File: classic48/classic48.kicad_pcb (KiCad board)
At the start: 2 copper layers, 3.4 x 3 mm, 5 parts, among them SW1 Switch, U1 RP2040_Pro_Micro, U2 TRRS

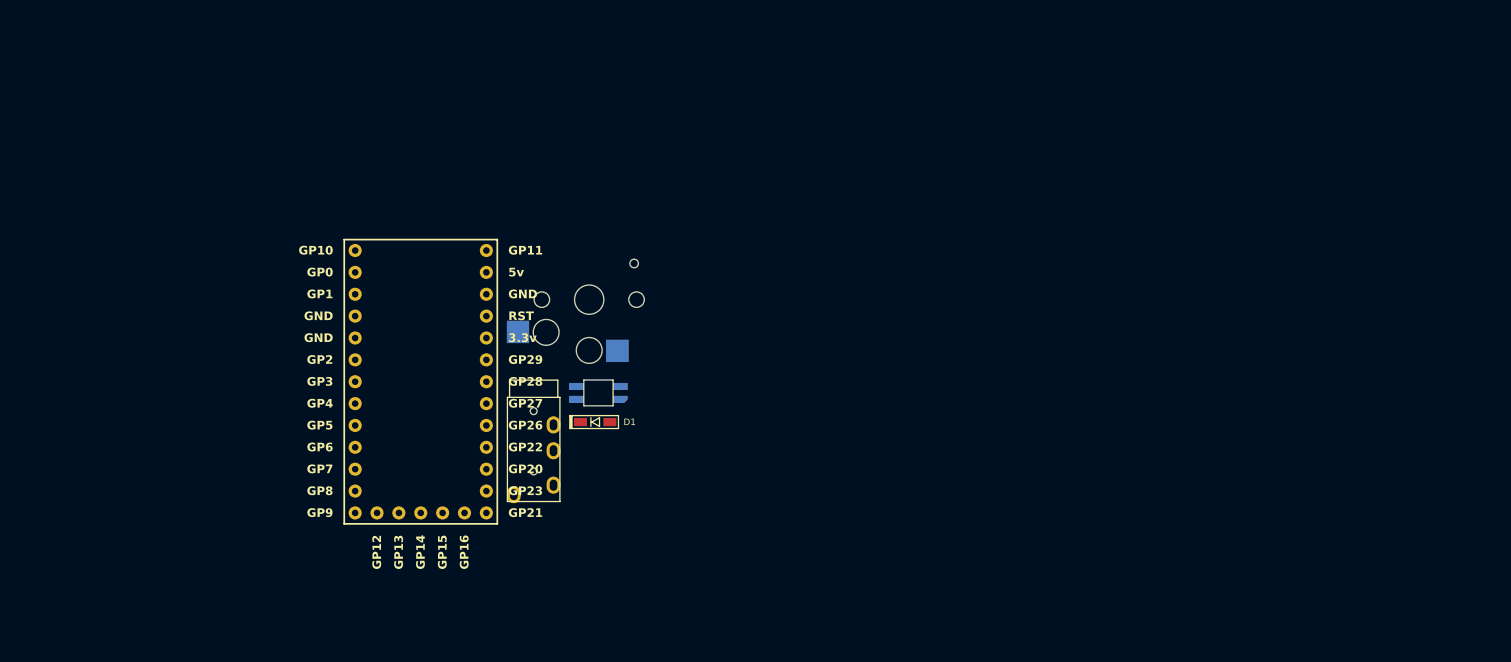
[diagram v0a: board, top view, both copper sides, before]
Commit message: feat: schematic for left side
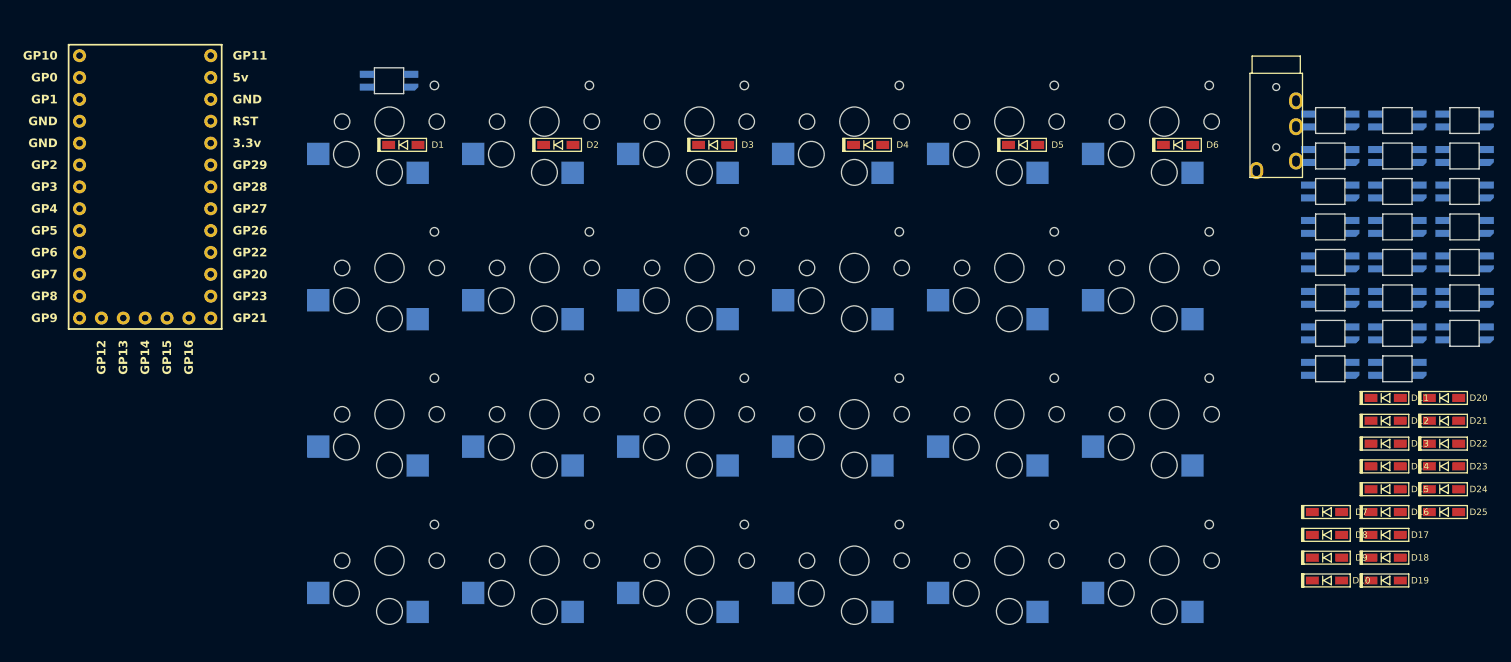
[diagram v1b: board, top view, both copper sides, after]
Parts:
- added D10: Diode_1N4148-SOD123, pjimenez:Diode_1N4148-SOD123, F.Cu at (165.9, 83.8)
- added D11: Diode_1N4148-SOD123, pjimenez:Diode_1N4148-SOD123, F.Cu at (172.7, 62.6)
- added D12: Diode_1N4148-SOD123, pjimenez:Diode_1N4148-SOD123, F.Cu at (172.7, 65.2)
- added D13: Diode_1N4148-SOD123, pjimenez:Diode_1N4148-SOD123, F.Cu at (172.7, 67.9)
- added D14: Diode_1N4148-SOD123, pjimenez:Diode_1N4148-SOD123, F.Cu at (172.7, 70.5)
- added D15: Diode_1N4148-SOD123, pjimenez:Diode_1N4148-SOD123, F.Cu at (172.7, 73.2)
- added D16: Diode_1N4148-SOD123, pjimenez:Diode_1N4148-SOD123, F.Cu at (172.7, 75.8)
- added D17: Diode_1N4148-SOD123, pjimenez:Diode_1N4148-SOD123, F.Cu at (172.7, 78.5)
- added D18: Diode_1N4148-SOD123, pjimenez:Diode_1N4148-SOD123, F.Cu at (172.7, 81.2)
- added D19: Diode_1N4148-SOD123, pjimenez:Diode_1N4148-SOD123, F.Cu at (172.7, 83.8)
- added D2: Diode_1N4148-SOD123, pjimenez:Diode_1N4148-SOD123, F.Cu at (76.6, 33.2)
- added D20: Diode_1N4148-SOD123, pjimenez:Diode_1N4148-SOD123, F.Cu at (179.5, 62.6)
- added D21: Diode_1N4148-SOD123, pjimenez:Diode_1N4148-SOD123, F.Cu at (179.5, 65.2)
- added D22: Diode_1N4148-SOD123, pjimenez:Diode_1N4148-SOD123, F.Cu at (179.5, 67.9)
- added D23: Diode_1N4148-SOD123, pjimenez:Diode_1N4148-SOD123, F.Cu at (179.5, 70.5)
- added D24: Diode_1N4148-SOD123, pjimenez:Diode_1N4148-SOD123, F.Cu at (179.5, 73.2)
- added D25: Diode_1N4148-SOD123, pjimenez:Diode_1N4148-SOD123, F.Cu at (179.5, 75.8)
- added D3: Diode_1N4148-SOD123, pjimenez:Diode_1N4148-SOD123, F.Cu at (94.6, 33.2)
- added D4: Diode_1N4148-SOD123, pjimenez:Diode_1N4148-SOD123, F.Cu at (112.6, 33.2)
- added D5: Diode_1N4148-SOD123, pjimenez:Diode_1N4148-SOD123, F.Cu at (130.6, 33.2)
- added D6: Diode_1N4148-SOD123, pjimenez:Diode_1N4148-SOD123, F.Cu at (148.6, 33.2)
- added D7: Diode_1N4148-SOD123, pjimenez:Diode_1N4148-SOD123, F.Cu at (165.9, 75.8)
- added D8: Diode_1N4148-SOD123, pjimenez:Diode_1N4148-SOD123, F.Cu at (165.9, 78.5)
- added D9: Diode_1N4148-SOD123, pjimenez:Diode_1N4148-SOD123, F.Cu at (165.9, 81.2)
- added LED10: LED_SK6812MINI-E, pjimenez:LED_SK6812-MINI-E, F.Cu at (174.1, 30.4)
- added LED11: LED_SK6812MINI-E, pjimenez:LED_SK6812-MINI-E, F.Cu at (174.1, 34.5)
- added LED12: LED_SK6812MINI-E, pjimenez:LED_SK6812-MINI-E, F.Cu at (174.1, 38.6)
- added LED13: LED_SK6812MINI-E, pjimenez:LED_SK6812-MINI-E, F.Cu at (174.1, 42.7)
- added LED14: LED_SK6812MINI-E, pjimenez:LED_SK6812-MINI-E, F.Cu at (174.1, 46.9)
- added LED15: LED_SK6812MINI-E, pjimenez:LED_SK6812-MINI-E, F.Cu at (174.1, 51.0)
- added LED16: LED_SK6812MINI-E, pjimenez:LED_SK6812-MINI-E, F.Cu at (174.1, 55.1)
- added LED17: LED_SK6812MINI-E, pjimenez:LED_SK6812-MINI-E, F.Cu at (174.1, 59.2)
- added LED18: LED_SK6812MINI-E, pjimenez:LED_SK6812-MINI-E, F.Cu at (181.9, 30.4)
- added LED19: LED_SK6812MINI-E, pjimenez:LED_SK6812-MINI-E, F.Cu at (181.9, 34.5)
- added LED2: LED_SK6812MINI-E, pjimenez:LED_SK6812-MINI-E, F.Cu at (166.3, 30.4)
- added LED20: LED_SK6812MINI-E, pjimenez:LED_SK6812-MINI-E, F.Cu at (181.9, 38.6)
- added LED21: LED_SK6812MINI-E, pjimenez:LED_SK6812-MINI-E, F.Cu at (181.9, 42.7)
- added LED22: LED_SK6812MINI-E, pjimenez:LED_SK6812-MINI-E, F.Cu at (181.9, 46.9)
- added LED23: LED_SK6812MINI-E, pjimenez:LED_SK6812-MINI-E, F.Cu at (181.9, 51.0)
- added LED24: LED_SK6812MINI-E, pjimenez:LED_SK6812-MINI-E, F.Cu at (181.9, 55.1)
- added LED3: LED_SK6812MINI-E, pjimenez:LED_SK6812-MINI-E, F.Cu at (166.3, 34.5)
- added LED4: LED_SK6812MINI-E, pjimenez:LED_SK6812-MINI-E, F.Cu at (166.3, 38.6)
- added LED5: LED_SK6812MINI-E, pjimenez:LED_SK6812-MINI-E, F.Cu at (166.3, 42.7)
- added LED6: LED_SK6812MINI-E, pjimenez:LED_SK6812-MINI-E, F.Cu at (166.3, 46.9)
- added LED7: LED_SK6812MINI-E, pjimenez:LED_SK6812-MINI-E, F.Cu at (166.3, 51.0)
- added LED8: LED_SK6812MINI-E, pjimenez:LED_SK6812-MINI-E, F.Cu at (166.3, 55.1)
- added LED9: LED_SK6812MINI-E, pjimenez:LED_SK6812-MINI-E, F.Cu at (166.3, 59.2)
- added SW10: Switch, pjimenez:Switch_ChocV1-hotswap, F.Cu at (111.0, 47.5)
- added SW11: Switch, pjimenez:Switch_ChocV1-hotswap, F.Cu at (129.0, 47.5)
- added SW12: Switch, pjimenez:Switch_ChocV1-hotswap, F.Cu at (147.0, 47.5)
- added SW13: Switch, pjimenez:Switch_ChocV1-hotswap, F.Cu at (57.0, 64.5)
- added SW14: Switch, pjimenez:Switch_ChocV1-hotswap, F.Cu at (75.0, 64.5)
- added SW15: Switch, pjimenez:Switch_ChocV1-hotswap, F.Cu at (93.0, 64.5)
- added SW16: Switch, pjimenez:Switch_ChocV1-hotswap, F.Cu at (111.0, 64.5)
- added SW17: Switch, pjimenez:Switch_ChocV1-hotswap, F.Cu at (129.0, 64.5)
- added SW18: Switch, pjimenez:Switch_ChocV1-hotswap, F.Cu at (147.0, 64.5)
- added SW19: Switch, pjimenez:Switch_ChocV1-hotswap, F.Cu at (57.0, 81.5)
- added SW2: Switch, pjimenez:Switch_ChocV1-hotswap, F.Cu at (75.0, 30.5)
- added SW20: Switch, pjimenez:Switch_ChocV1-hotswap, F.Cu at (75.0, 81.5)
- added SW21: Switch, pjimenez:Switch_ChocV1-hotswap, F.Cu at (93.0, 81.5)
- added SW22: Switch, pjimenez:Switch_ChocV1-hotswap, F.Cu at (111.0, 81.5)
- added SW23: Switch, pjimenez:Switch_ChocV1-hotswap, F.Cu at (129.0, 81.5)
- added SW24: Switch, pjimenez:Switch_ChocV1-hotswap, F.Cu at (147.0, 81.5)
- added SW3: Switch, pjimenez:Switch_ChocV1-hotswap, F.Cu at (93.0, 30.5)
- added SW4: Switch, pjimenez:Switch_ChocV1-hotswap, F.Cu at (111.0, 30.5)
- added SW5: Switch, pjimenez:Switch_ChocV1-hotswap, F.Cu at (129.0, 30.5)
- added SW6: Switch, pjimenez:Switch_ChocV1-hotswap, F.Cu at (147.0, 30.5)
- added SW7: Switch, pjimenez:Switch_ChocV1-hotswap, F.Cu at (57.0, 47.5)
- added SW8: Switch, pjimenez:Switch_ChocV1-hotswap, F.Cu at (75.0, 47.5)
- added SW9: Switch, pjimenez:Switch_ChocV1-hotswap, F.Cu at (93.0, 47.5)
- moved U2 94.1 mm to (160.0, 24.9)
- moved LED1 43.7 mm to (57.0, 25.8)
- moved U1 39.2 mm to (28.6, 39.4)
- moved D1 39.2 mm to (58.6, 33.2)
- moved SW1 31.1 mm to (57.0, 30.5)
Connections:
- D1 pad 1: unconnected-(D1-K-Pad1) -> Row 0 Left
- D1 pad 2: unconnected-(D1-A-Pad2) -> Net-(D1-A)
- LED1 pad 1: unconnected-(LED1-VDD-Pad1) -> Net-(D25-K)
- LED1 pad 2: unconnected-(LED1-DOUT-Pad2) -> Net-(LED1-DOUT)
- LED1 pad 3: unconnected-(LED1-VSS-Pad3) -> GND Left
- LED1 pad 4: unconnected-(LED1-DIN-Pad4) -> LED Data Left
- SW1 pad 1: unconnected-(SW1-Pad1) -> Net-(D1-A)
- SW1 pad 2: unconnected-(SW1-Pad2) -> Col 0 Left
- U1 pad 15: unconnected-(U1-GP13-Pad15) -> Row 3 Left
- U1 pad 16: unconnected-(U1-GP14-Pad16) -> Row 2 Left
- U1 pad 17: unconnected-(U1-GP15-Pad17) -> Row 1 Left
- U1 pad 18: unconnected-(U1-GP16-Pad18) -> Row 0 Left
- U1 pad 19: unconnected-(U1-GP21-Pad19) -> Serial data left
- U1 pad 20: unconnected-(U1-GP23-Pad20) -> LED Data Left
- U1 pad 21: unconnected-(U1-GP20-Pad21) -> Col 5 Left
- U1 pad 22: unconnected-(U1-GP22-Pad22) -> Col 4 Left
- U1 pad 23: unconnected-(U1-GP26-Pad23) -> Col 3 Left
- U1 pad 24: unconnected-(U1-GP27-Pad24) -> Col 2 Left
- U1 pad 25: unconnected-(U1-GP28-Pad25) -> Col 1 Left
- U1 pad 26: unconnected-(U1-GP29-Pad26) -> Col 0 Left
- U1 pad 29: unconnected-(U1-GND-Pad29) -> GND Left
- U1 pad 30: unconnected-(U1-5v-Pad30) -> 5V Left
- U2 pad 1: unconnected-(U2-SLEEVE-Pad1) -> GND Left
- U2 pad 3: unconnected-(U2-RING1-Pad3) -> Serial data left
- U2 pad 4: unconnected-(U2-RING2-Pad4) -> 5V Left

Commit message: feat: position all right side diodes
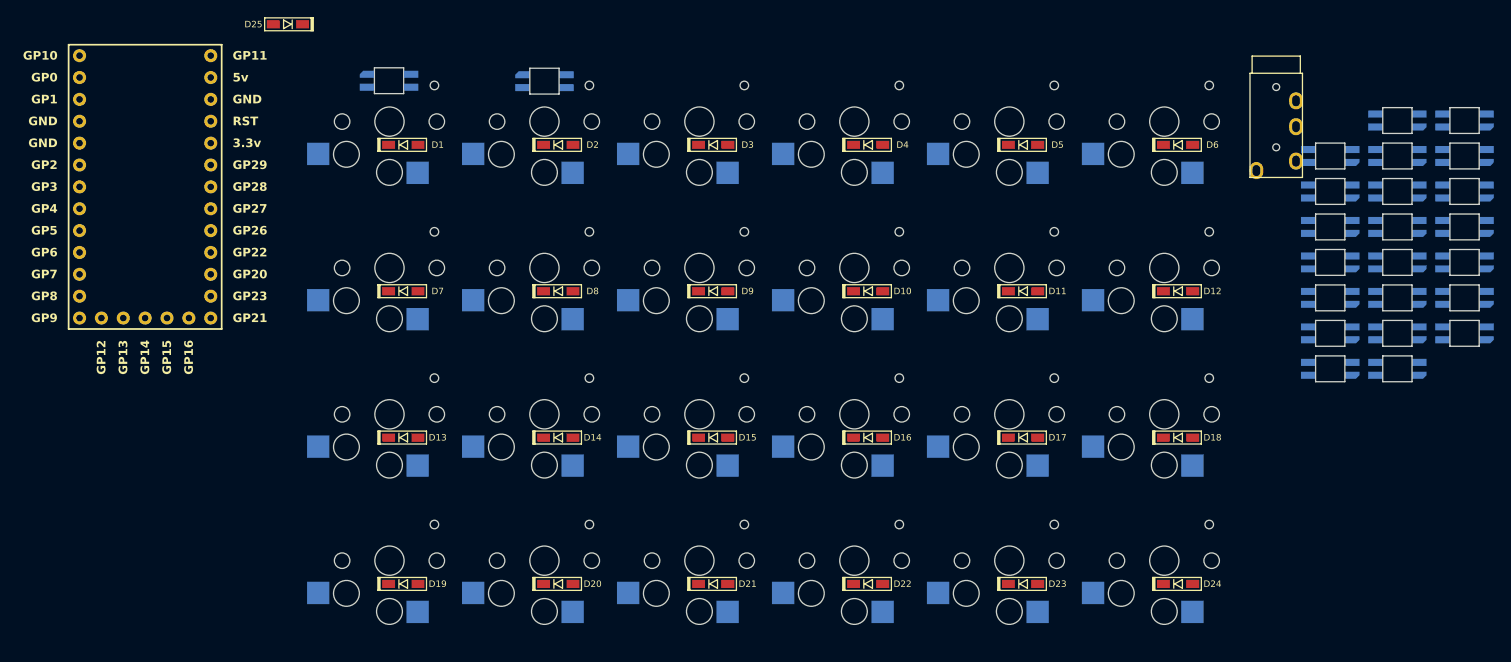
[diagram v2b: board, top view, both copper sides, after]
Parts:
- moved D25 145.8 mm to (45.2, 19.2), turned to 180 degrees
- moved D13 114.1 mm to (58.6, 67.2)
- moved D19 114.1 mm to (58.6, 84.2)
- moved D7 110.3 mm to (58.6, 50.2)
- moved D20 105.1 mm to (76.6, 84.2)
- moved D14 96.2 mm to (76.6, 67.2)
- moved D8 93.7 mm to (76.6, 50.2)
- moved LED2 91.4 mm to (75.0, 25.8), turned to 180 degrees
- moved D21 87.0 mm to (94.6, 84.2)
- moved D15 78.3 mm to (94.6, 67.2)
- moved D9 77.7 mm to (94.6, 50.2)
- moved D22 68.9 mm to (112.6, 84.2)
- moved D10 63.0 mm to (112.6, 50.2)
- moved D16 60.7 mm to (112.6, 67.2)
- moved D23 50.8 mm to (130.6, 84.2)
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
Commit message: fix: bring diodes to background
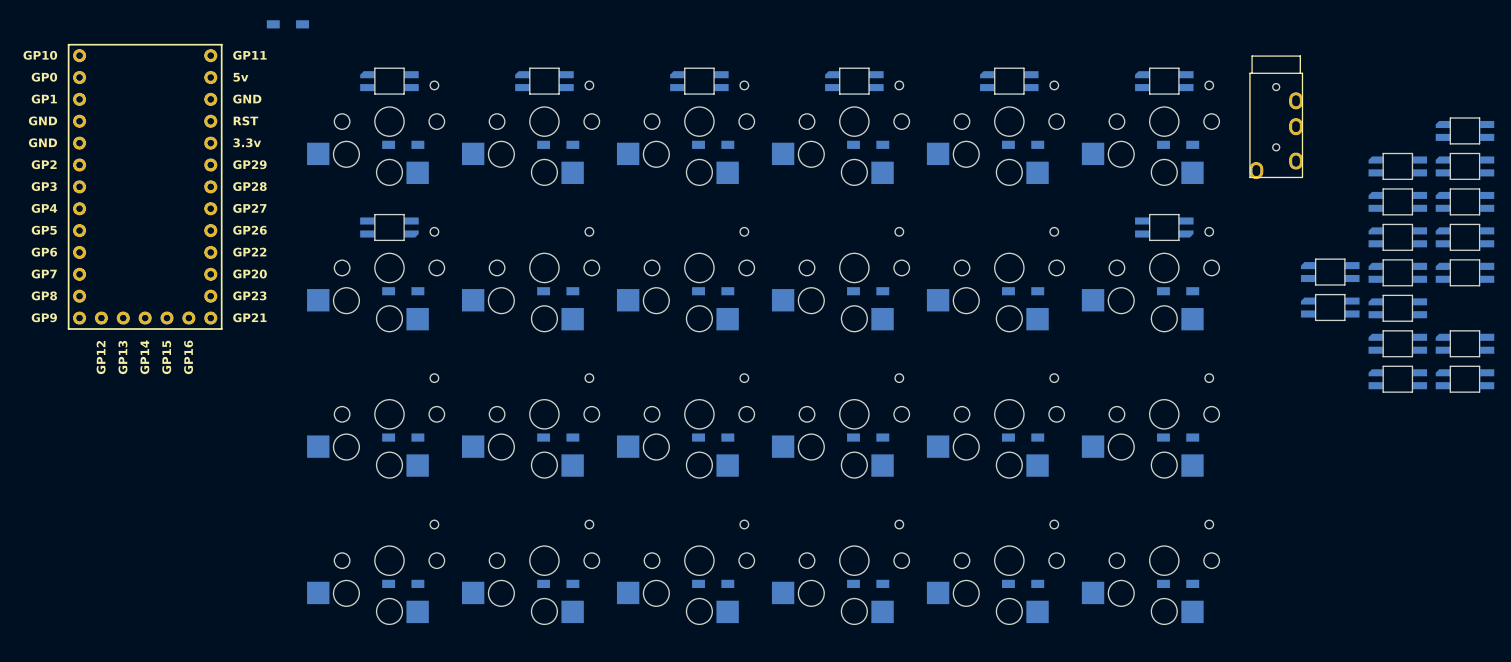
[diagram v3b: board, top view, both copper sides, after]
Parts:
- D1, D10, D11, D12, D13, D14, D15, D16, D17, D18, D19, D2, D20, D21, D22, D23, D24, D25, D3, D4, D5, D6, D7, D8, D9: moved to B.Cu
- moved LED12 117.1 mm to (57.0, 42.8)
- moved LED3 73.8 mm to (93.0, 25.8), turned to 180 degrees
- moved LED4 56.7 mm to (111.0, 25.8), turned to 180 degrees
- moved LED5 40.9 mm to (129.0, 25.8), turned to 180 degrees
- moved LED10 31.1 mm to (181.9, 60.4), turned to 180 degrees
- moved LED18 31.0 mm to (174.1, 60.4), turned to 180 degrees
- moved LED17 28.7 mm to (181.9, 31.6), turned to 180 degrees
- moved LED6 28.5 mm to (147.0, 25.8), turned to 180 degrees
- moved LED11 23.2 mm to (181.9, 56.3), turned to 180 degrees
- moved LED19 23.1 mm to (174.1, 56.3), turned to 180 degrees
- moved LED7 20.9 mm to (147.0, 42.8)
- moved LED16 20.9 mm to (181.9, 35.7), turned to 180 degrees
- moved LED24 20.9 mm to (174.1, 35.7), turned to 180 degrees
- moved LED20 15.6 mm to (174.1, 52.2), turned to 180 degrees
- moved LED15 13.6 mm to (181.9, 39.8), turned to 180 degrees
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
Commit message: feat: all LEDs in place
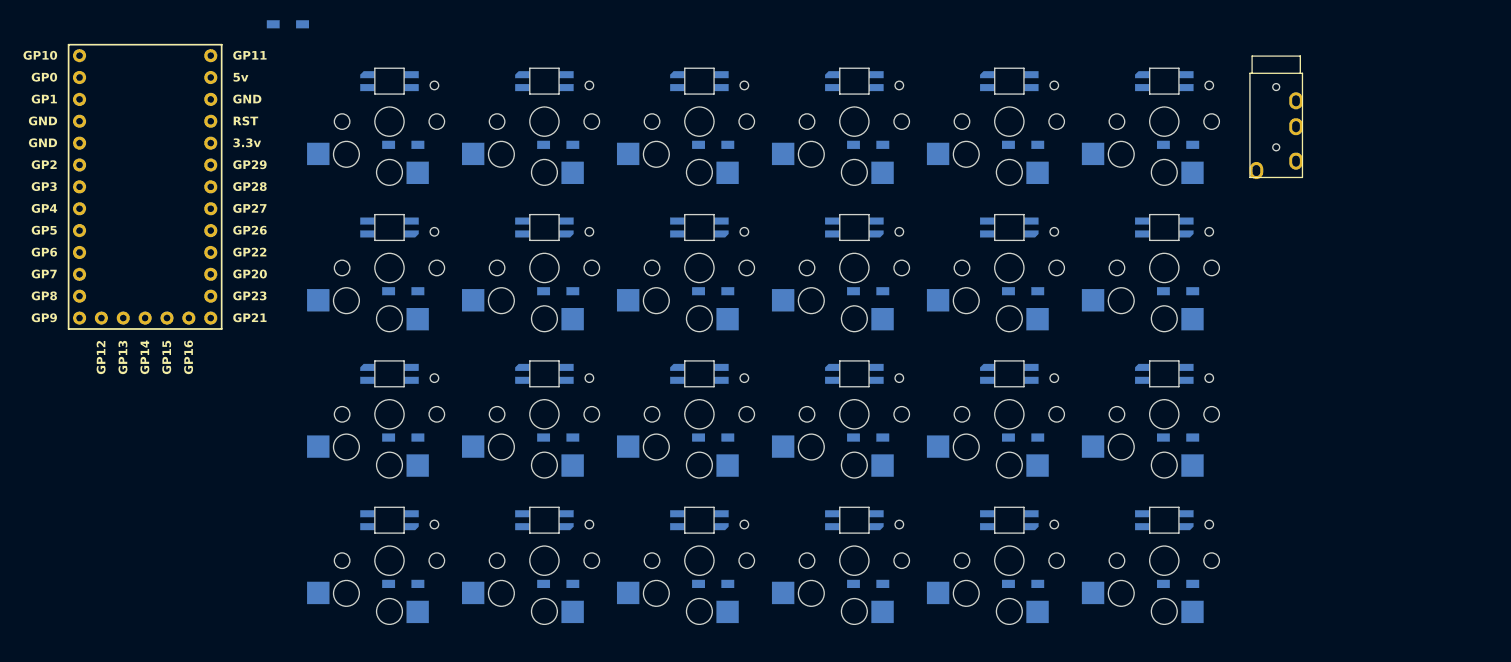
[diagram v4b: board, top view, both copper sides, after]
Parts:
- moved LED13 125.5 mm to (57.0, 59.8)
- moved LED24 124.1 mm to (57.0, 76.8), turned to 0 degrees
- moved LED14 108.1 mm to (75.0, 59.8)
- moved LED11 107.8 mm to (75.0, 42.8), turned to 0 degrees
- moved LED23 105.8 mm to (75.0, 76.8), turned to 0 degrees
- moved LED15 91.1 mm to (93.0, 59.8)
- moved LED10 90.7 mm to (93.0, 42.8), turned to 0 degrees
- moved LED22 87.5 mm to (93.0, 76.8), turned to 0 degrees
- moved LED16 74.9 mm to (111.0, 59.8)
- moved LED21 69.4 mm to (111.0, 76.8), turned to 0 degrees
- moved LED17 60.0 mm to (129.0, 59.8)
- moved LED9 55.5 mm to (111.0, 42.8), turned to 0 degrees
- moved LED20 51.4 mm to (129.0, 76.8), turned to 0 degrees
- moved LED8 38.4 mm to (129.0, 42.8), turned to 0 degrees
- moved LED19 34.0 mm to (147.0, 76.8), turned to 0 degrees
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
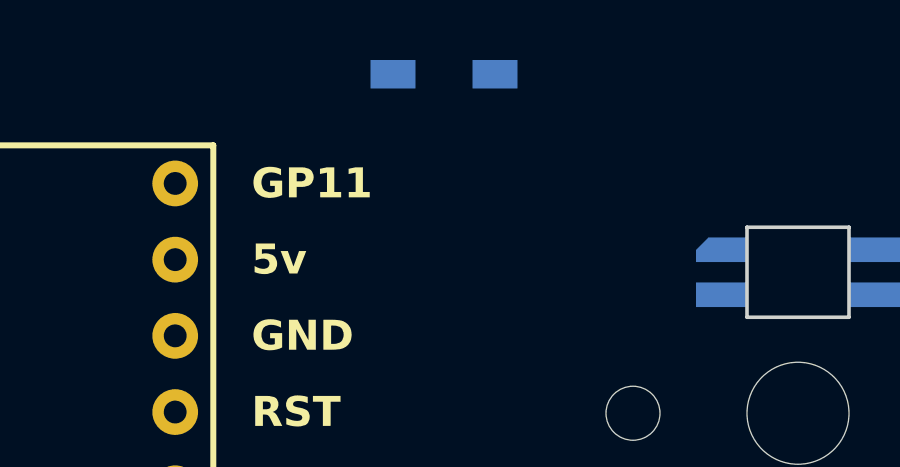
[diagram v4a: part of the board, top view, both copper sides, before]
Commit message: feat: add GND marker to 6812
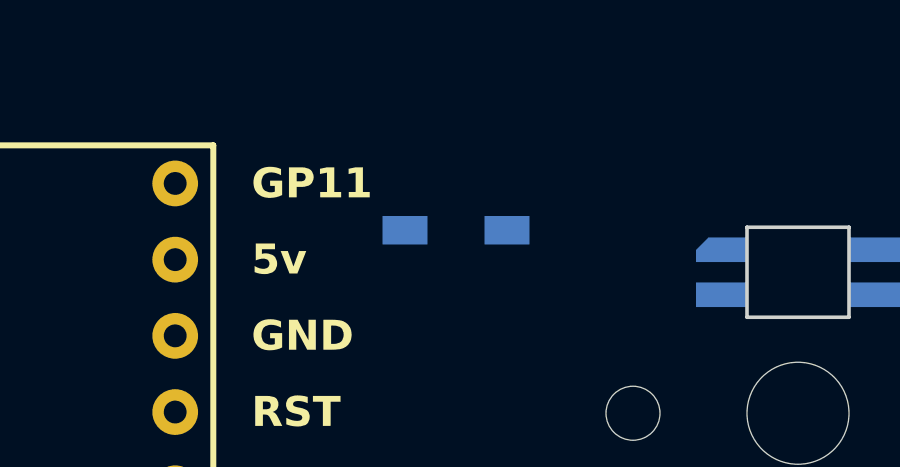
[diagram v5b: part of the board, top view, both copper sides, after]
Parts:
- D1, D10, D11, D12, D13, D14, D15, D16, D17, D18, D19, D2, D20, D21, D22, D23, D24, D25, D3, D4, D5, D6, D7, D8, D9: value Diode_1N4148-SOD123 -> D_Small
- moved D25 5.22 mm to (45.6, 24.4)

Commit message: feat: LED Vcc
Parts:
- moved D25 20.4 mm to (66.0, 23.0)
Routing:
- net 5V Left: track 0.00 -> 496.9 mm, vias 0 -> 6
- net Net-(LED18-DOUT): track 0.00 -> 22.3 mm
- net Net-(LED6-DOUT): track 0.00 -> 22.1 mm
- net GND Left: track 0.00 -> 19.4 mm
- net Net-(LED12-DOUT): track 0.00 -> 18.2 mm
- net Net-(LED8-DOUT): track 0.00 -> 13.5 mm
- net Net-(LED4-DOUT): track 0.00 -> 13.5 mm
- net Net-(LED3-DOUT): track 0.00 -> 13.5 mm
- net Net-(LED23-DOUT): track 0.00 -> 13.5 mm
- net Net-(LED22-DOUT): track 0.00 -> 13.5 mm
- net Net-(LED21-DOUT): track 0.00 -> 13.5 mm
- net Net-(LED20-DOUT): track 0.00 -> 13.5 mm
- net Net-(LED2-DOUT): track 0.00 -> 13.5 mm
- net Net-(LED16-DOUT): track 0.00 -> 13.5 mm
- net Net-(LED15-DOUT): track 0.00 -> 13.5 mm
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
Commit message: feat: LEDs and TRRS fully connected
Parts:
- D1, D10, D11, D12, D13, D14, D15, D16, D17, D18, D19, D2, D20, D21, D22, D23, D24, D25, D3, D4, D5, D6, D7, D8, D9: value D_Small -> Diode_1N4148-SOD123
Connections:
- U1 pad 19: Serial data left -> Col 5 Left
- U1 pad 20: LED Data Left -> Col 4 Left
- U1 pad 21: Col 5 Left -> Col 3 Left
- U1 pad 22: Col 4 Left -> Col 2 Left
- U1 pad 23: Col 3 Left -> Col 1 Left
- U1 pad 24: Col 2 Left -> Col 0 Left
- U1 pad 25: Col 1 Left -> Serial data left
- U1 pad 26: Col 0 Left -> LED Data Left
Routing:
- net GND Left: track 19.4 -> 507.9 mm, vias 0 -> 4
- net Serial data left: track 0.00 -> 130.9 mm, vias 0 -> 2
- net LED Data Left: track 0.00 -> 21.9 mm
- net Net-(D25-K): track 10.6 -> 11.3 mm
